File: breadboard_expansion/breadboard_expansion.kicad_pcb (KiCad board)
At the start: 2 copper layers, 27.9 x 53.3 mm, 12 parts, among them J1 Conn_01x02_Male, J2 Conn_01x02_Male, J3 Conn_01x02_Male, J4 Conn_01x02_Male

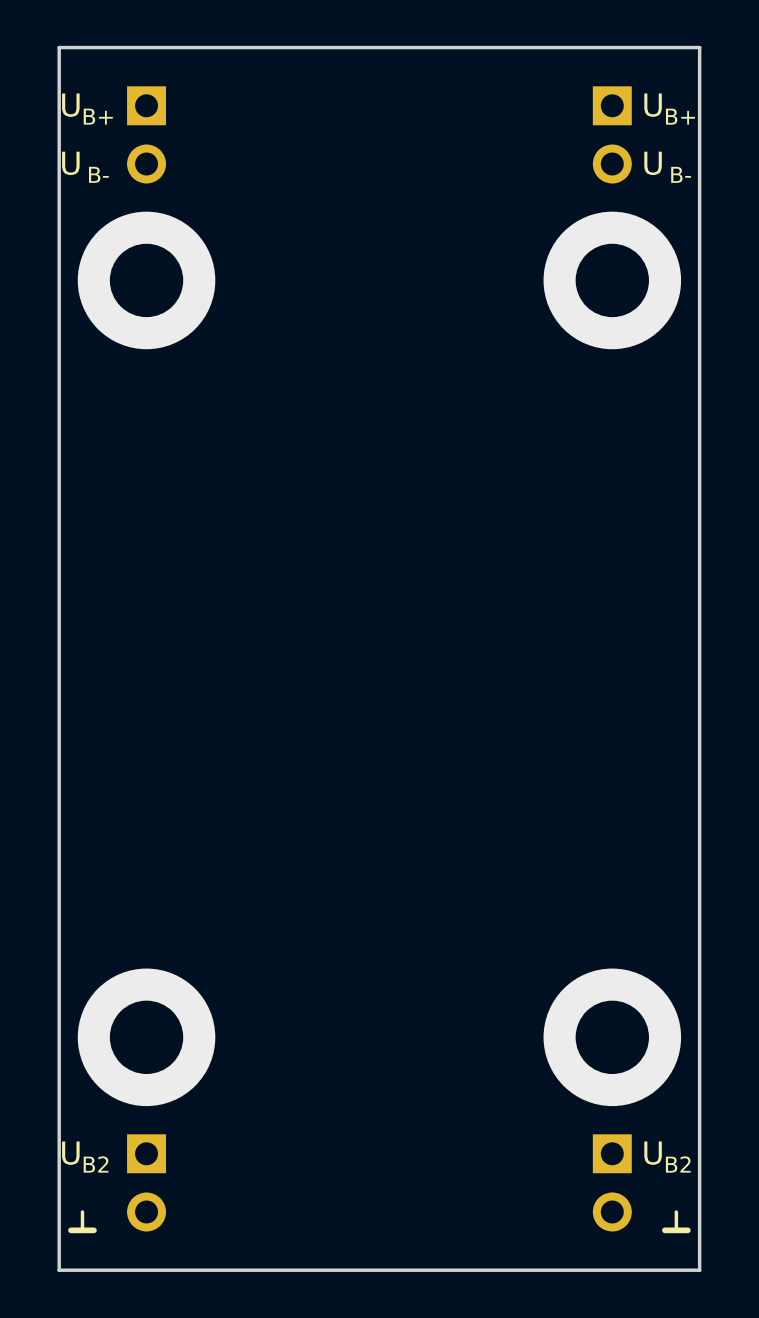
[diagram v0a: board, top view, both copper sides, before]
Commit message: Increase PCB width of base format.
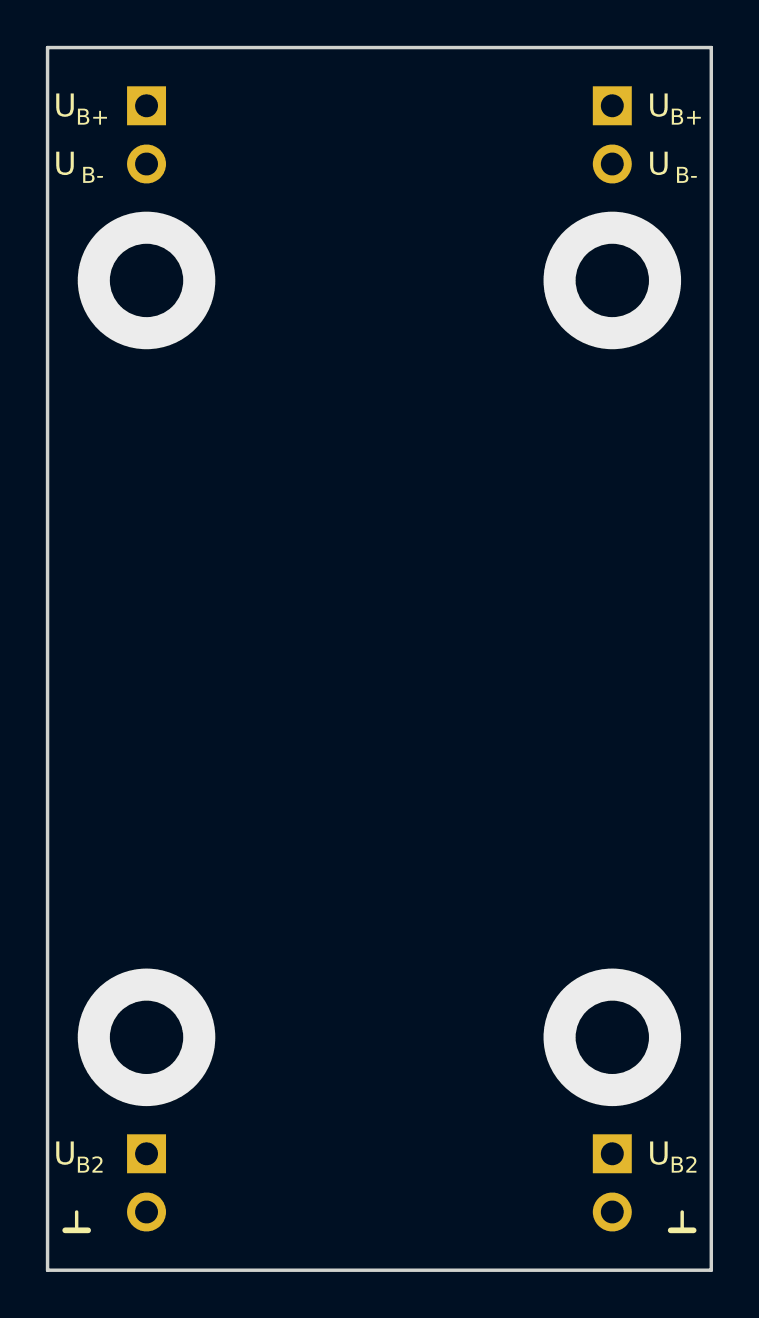
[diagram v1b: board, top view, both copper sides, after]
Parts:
- moved REF** 0.25 mm to (75.2, 91.4)
- moved REF** 0.25 mm to (75.2, 94.0)
- moved REF** 0.25 mm to (75.2, 137.2)
- moved REF** 0.25 mm to (75.7, 139.7)
- moved REF** 0.25 mm to (101.1, 91.4)
- moved REF** 0.25 mm to (101.1, 94.0)
- moved REF** 0.25 mm to (101.1, 137.2)
- moved REF** 0.25 mm to (102.1, 139.7)
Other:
- board size 27.9 x 53.3 mm -> 29 x 53.3 mm
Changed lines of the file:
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@@
   )
   (module Symbol-emt:Text_U_B+_Silkscreen (layer F.Cu)
-    (at 75.438 91.44)
+    (at 75.184 91.44)
     (descr "Voltage Label Betriebsspannung")
     (tags "Voltage Label Betriebsspannung")
@@
   )
   (module Symbol-emt:Text_U_B-_Silkscreen (layer F.Cu)
-    (at 75.438 93.98)
+    (at 75.184 93.98)
     (descr "Voltage Label Betriebsspannung")
     (tags "Voltage Label Betriebsspannung")
@@
   )
   (module Symbol-emt:Text_U_B2_Silkscreen (layer F.Cu)
-    (at 75.438 137.16)
+    (at 75.184 137.16)
     (descr "Voltage Label Betriebsspannung")
     (tags "Voltage Label Betriebsspannung")
@@
   )
   (module Symbol-emt:Symbol_GND_Silkscreen (layer F.Cu)
-    (at 75.946 139.7)
+    (at 75.692 139.7)
     (descr "Symbol GND")
     (tags "Symbol GND")
@@
   )
   (module Symbol-emt:Text_U_B+_Silkscreen (layer F.Cu)
-    (at 100.838 91.44)
+    (at 101.092 91.44)
     (descr "Voltage Label Betriebsspannung")
     (tags "Voltage Label Betriebsspannung")
@@
   )
   (module Symbol-emt:Text_U_B-_Silkscreen (layer F.Cu)
-    (at 100.838 93.98)
+    (at 101.092 93.98)
     (descr "Voltage Label Betriebsspannung")
     (tags "Voltage Label Betriebsspannung")
@@
   )
   (module Symbol-emt:Text_U_B2_Silkscreen (layer F.Cu)
-    (at 100.838 137.16)
+    (at 101.092 137.16)
     (descr "Voltage Label Betriebsspannung")
     (tags "Voltage Label Betriebsspannung")
@@
   )
   (module Symbol-emt:Symbol_GND_Silkscreen (layer F.Cu)
-    (at 101.854 139.7)
+    (at 102.108 139.7)
     (descr "Symbol GND")
     (tags "Symbol GND")
@@
     (fp_line (start -0.5 0.8) (end 0.5 0.8) (layer F.SilkS) (width 0.25))
   )
-  (gr_line (start 102.87 88.9) (end 102.87 142.24) (layer Edge.Cuts) (width 0.15))
-  (gr_line (start 74.93 142.24) (end 102.87 142.24) (layer Edge.Cuts) (width 0.15))
-  (gr_line (start 74.93 88.9) (end 102.87 88.9) (layer Edge.Cuts) (width 0.15))
-  (gr_line (start 74.93 88.9) (end 74.93 142.24) (layer Edge.Cuts) (width 0.15))
+  (gr_line (start 103.378 88.9) (end 103.378 142.24) (layer Edge.Cuts) (width 0.15))
+  (gr_line (start 74.422 142.24) (end 103.378 142.24) (layer Edge.Cuts) (width 0.15))
+  (gr_line (start 74.422 88.9) (end 103.378 88.9) (layer Edge.Cuts) (width 0.15))
+  (gr_line (start 74.422 88.9) (end 74.422 142.24) (layer Edge.Cuts) (width 0.15))
   (via (at 78.74 99.06) (size 6) (drill 3.2) (layers F.Cu B.Cu) (net 0) (status 40000))
   (via (at 99.06 99.06) (size 6) (drill 3.2) (layers F.Cu B.Cu) (net 0) (status 40000))
